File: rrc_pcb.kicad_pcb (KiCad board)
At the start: 2 copper layers, 149.9 x 78.4 mm, 15 parts, among them J1 Conn_01x02_Male-Connector, J2 Conn_01x03_Male-Connector, J3 Conn_01x02_Male-Connector, J4 Conn_01x02_Female, U1 iridium9602, U2 Teensy4.1, U3 BN220-GPS, U4 ICM-20948, U5 MS5611, U6 logo

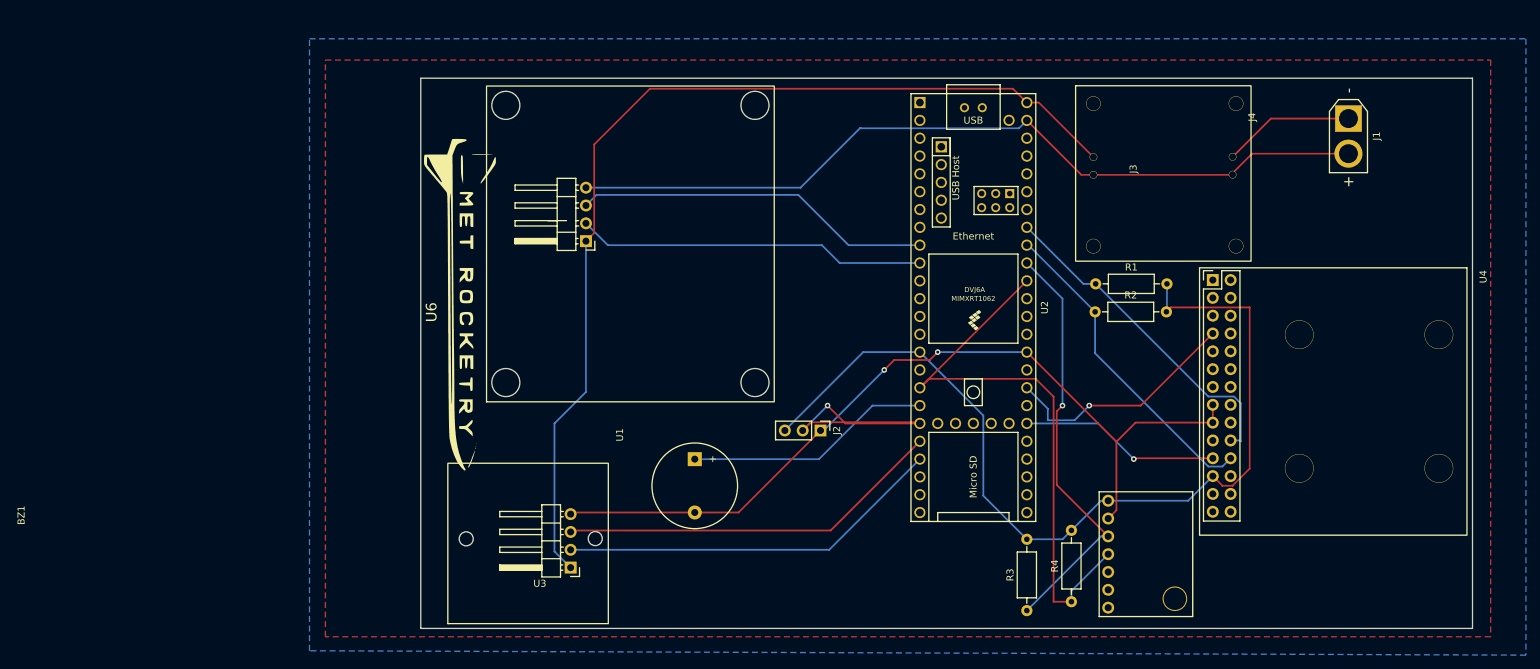
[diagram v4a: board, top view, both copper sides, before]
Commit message: PCB is now ready to fabricate
added gerbers and traces
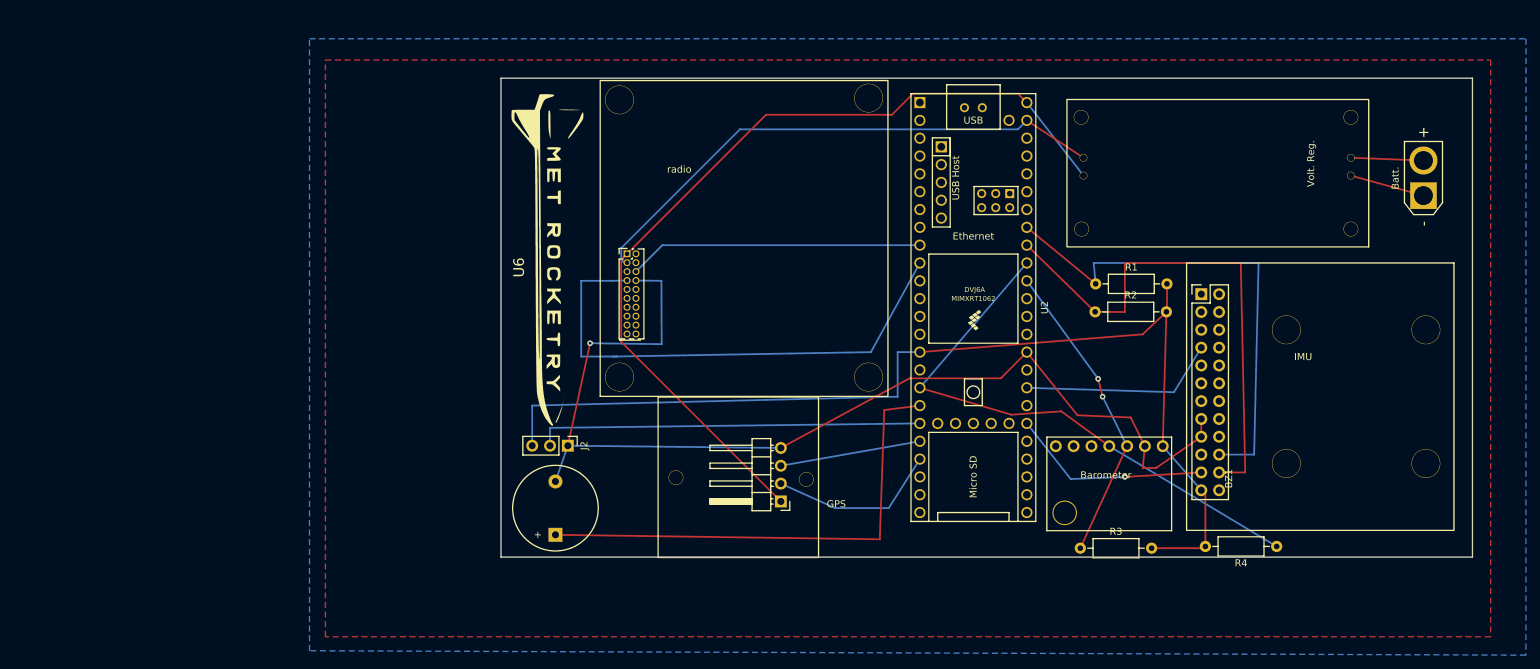
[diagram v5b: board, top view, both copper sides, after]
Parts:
- removed J3: Conn_01x02_Male-Connector, Connector_PinSocket_2.54mm:PinSocket_1x02_P2.54mm_Horizontal
- removed J4: Conn_01x02_Female, Connector_PinSocket_2.54mm:PinSocket_2x01_P2.54mm_Horizontal
- added Volt. Reg.: Conn_01x02_Male-Connector, VoltReg:voltReg, F.Cu at (165.6, 44.7)
- GPS: renamed from U3; footprint Connector_PinHeader_2.54mm:PinHeader_1x04_P2.54mm_Horizontal -> bn220_gps:BN220
- IMU: renamed from U4; footprint Connector_PinHeader_2.54mm:PinHeader_2x14_P2.54mm_Vertical -> icm20948:icm20948
- radio: renamed from U1; footprint Connector_PinHeader_2.54mm:PinHeader_1x04_P2.54mm_Horizontal -> iridium9602:iridium9602
- moved radio 49.0 mm to (56.4, 20.6), turned to 0 degrees
- moved GPS 44.0 mm to (64.3, 66.1), turned to 0 degrees
- moved J2 36.1 mm to (51.4, 73.0)
- moved R4 30.3 mm to (152.4, 87.4), turned to 180 degrees
- moved IMU 26.8 mm to (156.2, 60.9), turned to 0 degrees
- moved BZ1 22.6 mm to (49.7, 85.7), turned to 90 degrees
- moved Barometer 19.6 mm to (128.6, 69.3), turned to 180 degrees
- moved Batt. 15.3 mm to (173.4, 37.4), turned to 90 degrees
- moved U6 14.0 mm to (48.7, 43.6)
- moved R3 11.7 mm to (124.5, 87.6), turned to 0 degrees
- renumbered U5 to Barometer, J1 to Batt.
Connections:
- net RX1 renamed RX7
- net SCL2 renamed SCL
- net SDA2 renamed SDA
- net TX1 renamed TX7
- Batt. pad 1: 7.2V -> Net-(J1-Pad1)
- Batt. pad 2: GND -> Net-(J1-Pad2)
- IMU pad 9: (no net) -> unconnected-(U4-Pad9)
- U2 pad 38: SDA1 -> SCL1
- U2 pad 39: SCL1 -> SDA1
- radio pad 2: TX2 -> unconnected-(U1-Pad2)
- radio pad 3: RX2 -> GND
- radio pad 4: GND -> unconnected-(U1-Pad4)
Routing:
- net GND: track 117.1 -> 77.7 mm
- net RX7: track 55.1 -> 20.1 mm
- net Net-(BZ1-Pad1): track 35.2 -> 69.8 mm
- net TX7: track 55.1 -> 24.4 mm
- net T_GND: track 121.5 -> 151.7 mm, vias 2 -> 1
- net SDA: track 46.1 -> 74.9 mm
- net TX2: track 49.9 -> 73.7 mm
- net SCL: track 47.8 -> 71.5 mm
- net 7.2V: track 18.8 -> 0.00 mm
- net Net-(J2-Pad2): track 36.5 -> 55.2 mm, vias 1 -> 0
- net T_VCC: track 133.0 -> 151.4 mm
- net VCC: track 142.1 -> 125.2 mm
- net SCL1: track 60.4 -> 43.8 mm, vias 1 -> 2
- net Net-(J1-Pad1): track 0.00 -> 10.7 mm
- net Net-(J1-Pad2): track 0.00 -> 10.4 mm
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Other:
- board size 149.9 x 78.4 mm -> 138.4 x 68.2 mm

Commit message: tweaked srad main board
tweaked iridium footprints and volt reg footprints and added a back board just in case iridium doenst pan out; uses rfd900p instead.
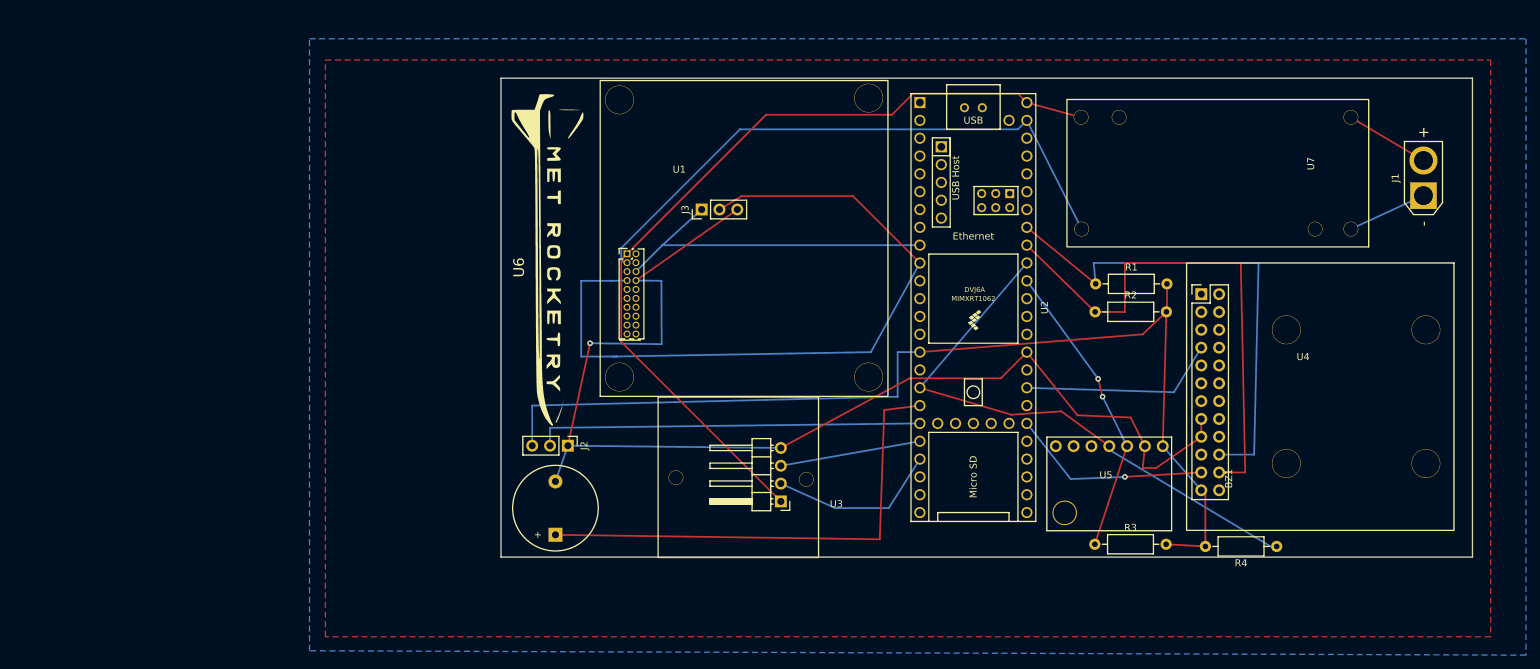
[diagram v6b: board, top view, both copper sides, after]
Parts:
- added J3: digital logic connection, Connector_PinHeader_2.54mm:PinHeader_1x03_P2.54mm_Vertical, F.Cu at (70.5, 39.4)
- U7: renamed from Volt. Reg.
- moved R3 2.14 mm to (126.5, 87.1)
- renumbered Batt. to J1, radio to U1, GPS to U3, IMU to U4, Barometer to U5
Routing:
- net TX2: track 73.7 -> 106.8 mm
- net T_GND: track 151.7 -> 169.4 mm
- net GND: track 77.7 -> 85.3 mm
- net RX2: track 42.0 -> 49.6 mm
- net VCC: track 125.2 -> 120.0 mm
- net T_VCC: track 151.4 -> 149.5 mm
- net Net-(J1-Pad2): track 10.4 -> 12.0 mm
- net SCL1: track 43.8 -> 42.5 mm
- net Net-(J1-Pad1): track 10.7 -> 11.4 mm

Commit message: Edit of PCB
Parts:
- removed U1: iridium9602, iridium9602:iridium9602
- added RF1: RFD900+-RF_Module, rfd900+:RFD900+, F.Cu at (57.0, 23.9)
- U7: value Conn_01x02_Male-Connector -> voltReg
- moved U6 122.3 mm to (168.6, 67.7), turned to 90 degrees
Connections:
- U4 pad 24: unconnected-(U4-Pad24) -> VCC
